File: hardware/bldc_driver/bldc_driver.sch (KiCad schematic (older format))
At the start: 0 parts

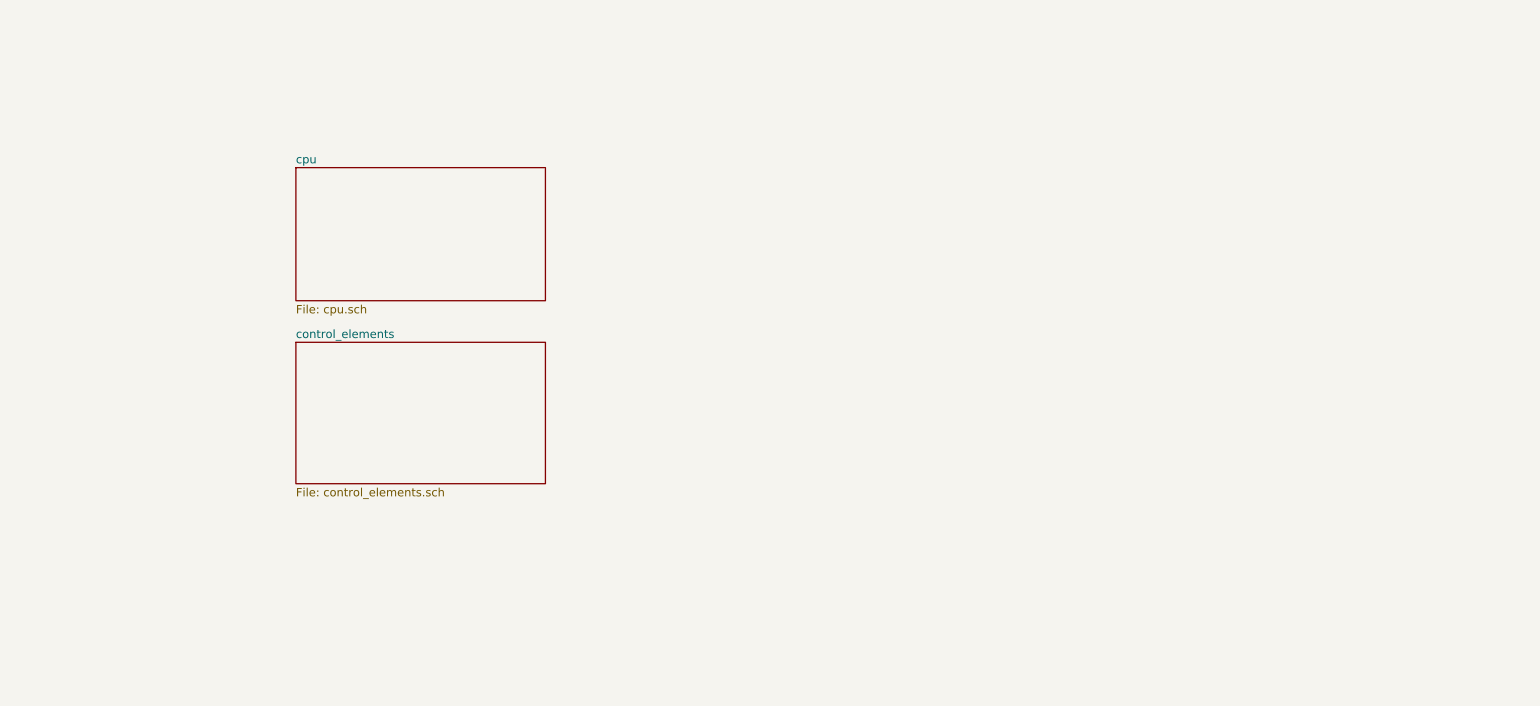
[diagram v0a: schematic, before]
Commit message: Cosmetic - trace improvements
- correcting 3-way trace intersections
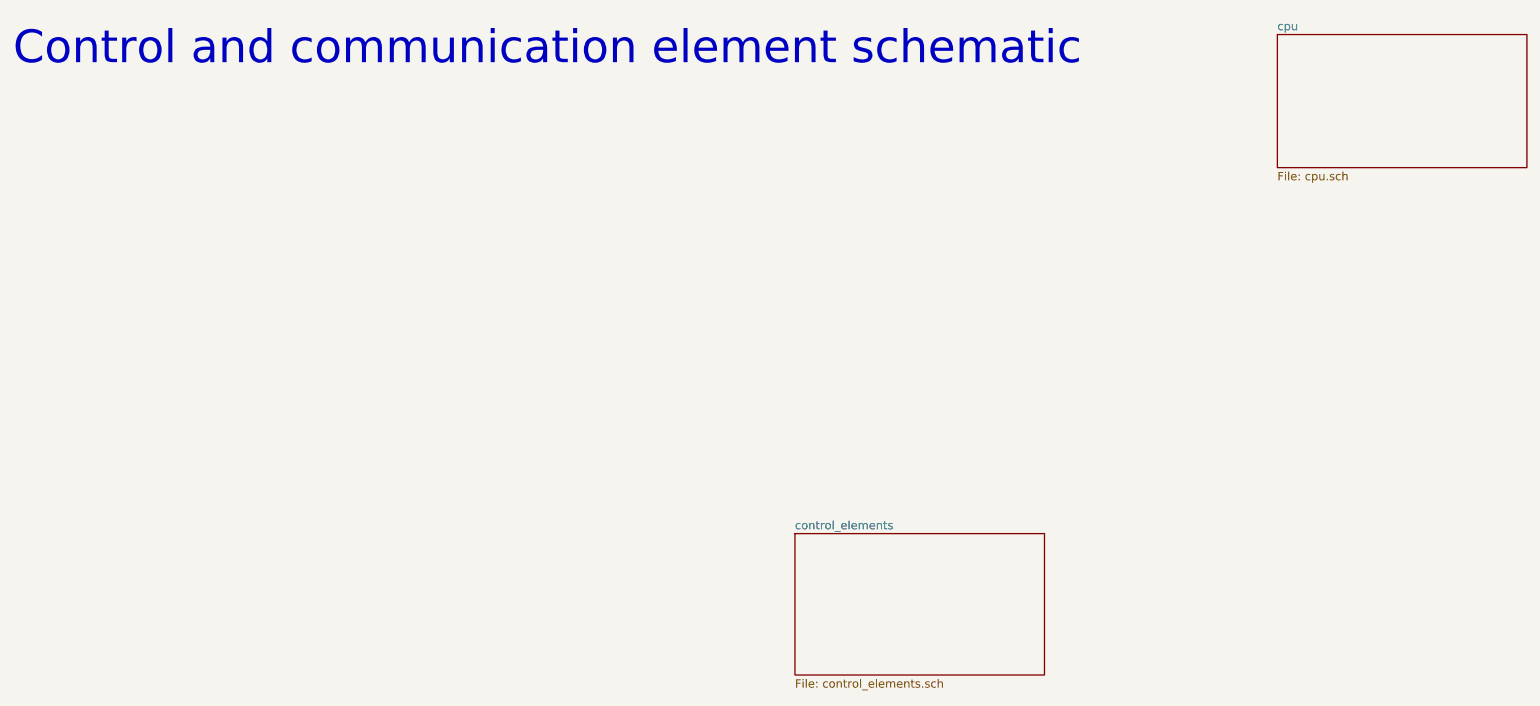
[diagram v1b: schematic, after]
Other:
- note added: "Control and communication element schematic\n"
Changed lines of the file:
@@
 $EndDescr
 $Sheet
-S 2450 1550 1500 800
+S 8350 750  1500 800
 U 6114126B
 F0 "cpu" 50
@@
 $EndSheet
 $Sheet
-S 2450 2600 1500 850
+S 5450 3750 1500 850
 U 6114135B
 F0 "control_elements" 50
 F1 "control_elements.sch" 50
 $EndSheet
+Text Notes 750  950  0    197  ~ 0
+Control and communication element schematic\n
 $EndSCHEMATC
